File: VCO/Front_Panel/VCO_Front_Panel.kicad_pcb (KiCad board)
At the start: 2 copper layers, 50.3 x 128.5 mm, 5 parts

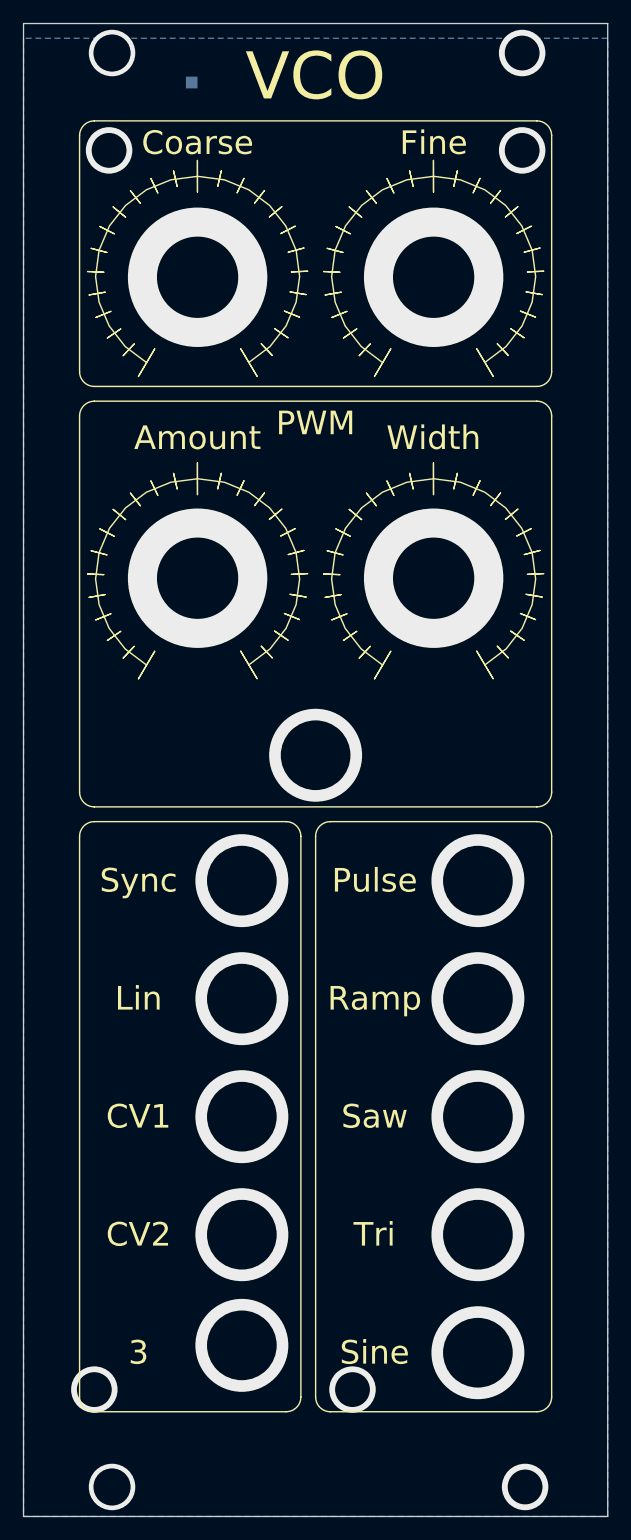
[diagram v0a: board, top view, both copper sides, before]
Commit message: Resolve most of the issues in known_issues.txt
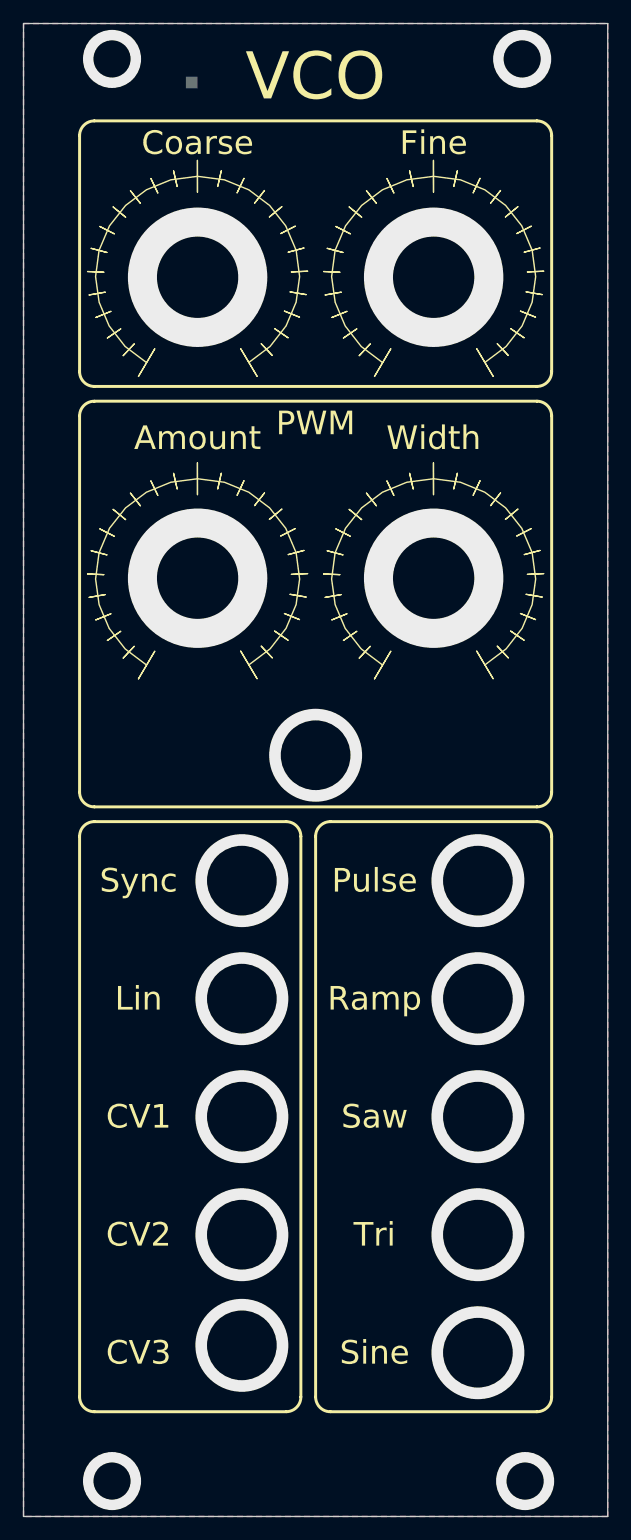
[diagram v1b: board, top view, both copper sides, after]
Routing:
- net GND: vias 23 -> 19
- added copper zone on F.Cu, net GND
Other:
- board text added: "CV3"
- board text removed: "3"

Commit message: Fix minor issues with VCO board
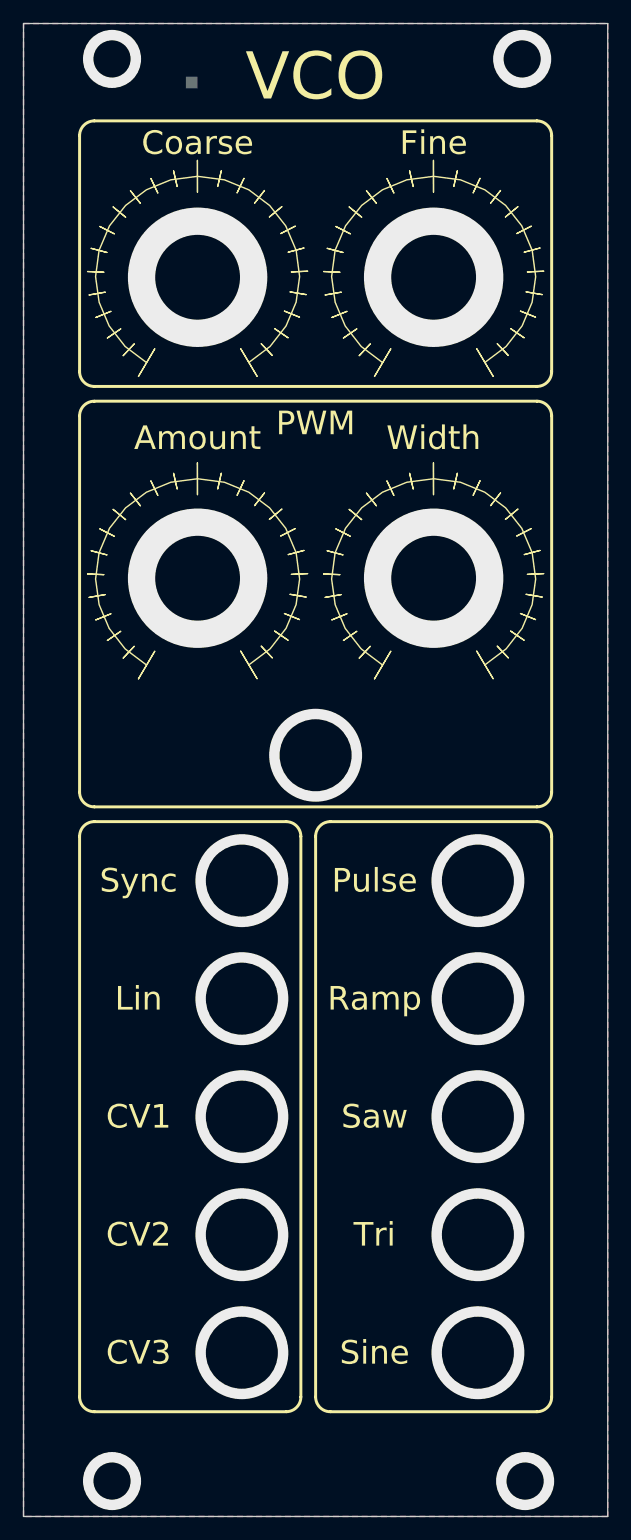
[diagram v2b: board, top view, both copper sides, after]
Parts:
- added REF**: OSHW-Logo2_7.3x6mm_SilkScreen, Symbol:OSHW-Logo2_7.3x6mm_SilkScreen, B.Cu at (97.3, 44.5)
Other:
- board text added: "WH"

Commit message: Bunch of bug fixes and tweaks
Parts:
- removed TP1: TestPoint, TestPoint:TestPoint_Pad_1.0x1.0mm
- added H1: Top_MH1, Eurorack:eurorack_mounting_hole, F.Cu at (71.4, 42.9)
- added H10: Ramp, Eurorack:jack_fp_hole, F.Cu at (102.9, 123.8)
- added H11: Saw, Eurorack:jack_fp_hole, F.Cu at (102.9, 134.0)
- added H12: PWM_Mod, Eurorack:jack_fp_hole, F.Cu at (88.9, 102.9)
- added H13: CV1, Eurorack:jack_fp_hole, F.Cu at (82.5, 134.0)
- added H14: Tri, Eurorack:jack_fp_hole, F.Cu at (102.9, 144.1)
- added H15: CV2, Eurorack:jack_fp_hole, F.Cu at (82.5, 144.1)
- added H16: Sine, Eurorack:jack_fp_hole, F.Cu at (102.9, 154.3)
- added H17: CV3, Eurorack:jack_fp_hole, F.Cu at (82.5, 154.3)
- added H18: Top_MH2, Eurorack:eurorack_mounting_hole, F.Cu at (106.7, 42.9)
- added H19: Bottom_MH2, Eurorack:eurorack_mounting_hole, F.Cu at (106.9, 165.4)
- added H2: Bottom_MH1, Eurorack:eurorack_mounting_hole, F.Cu at (71.4, 165.4)
- added H3: Coarse, Eurorack:pot_fp_hole, F.Cu at (78.7, 61.7)
- added H4: PWM_Amt, Eurorack:pot_fp_hole, F.Cu at (78.7, 87.6)
- added H5: Sync, Eurorack:jack_fp_hole, F.Cu at (82.5, 113.7)
- added H6: Pulse, Eurorack:jack_fp_hole, F.Cu at (102.9, 113.7)
- added H7: Fine, Eurorack:pot_fp_hole, F.Cu at (99.1, 61.7)
- added H8: PWM_Width, Eurorack:pot_fp_hole, F.Cu at (99.1, 87.6)
- added H9: Lin, Eurorack:jack_fp_hole, F.Cu at (82.5, 123.8)
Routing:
- net GND: vias 19 -> 0

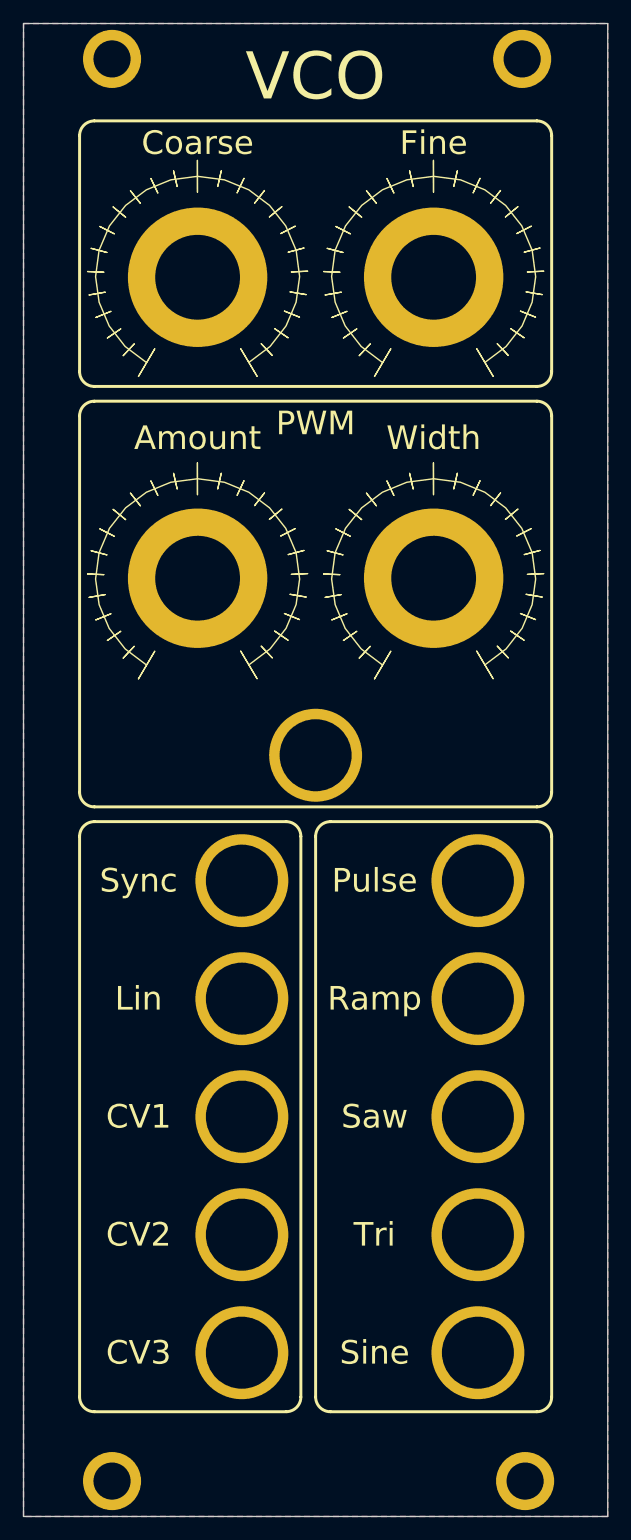
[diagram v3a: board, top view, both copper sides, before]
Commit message: Clean up layout of VCO board
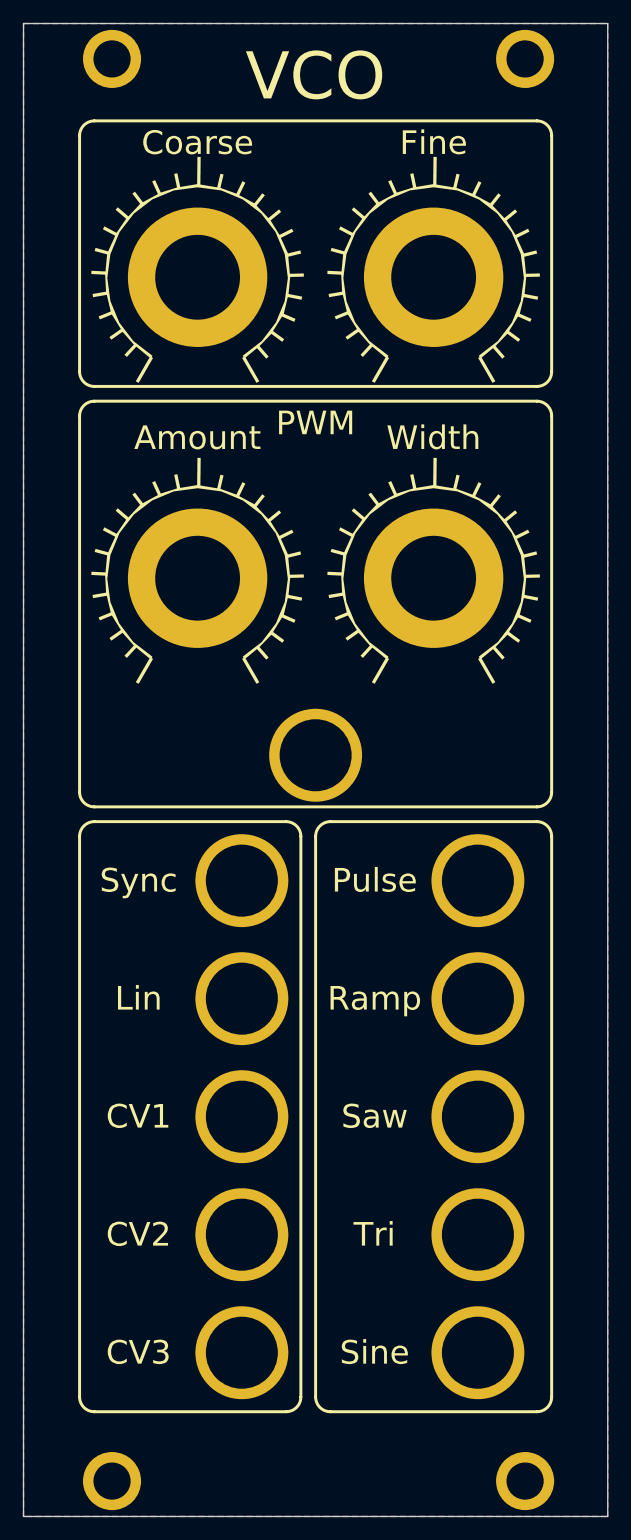
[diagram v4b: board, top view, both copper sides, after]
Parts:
- removed tick_marks (x4): G***, AS3340_VCO_FP:knob_tick_marks
- added svg2mod: G***, Eurorack:knob_tick_marks, F.Cu at (78.7, 87.0)
- added svg2mod: G***, Eurorack:knob_tick_marks, F.Cu at (99.1, 87.0)
- added svg2mod: G***, Eurorack:knob_tick_marks, F.Cu at (78.7, 61.1)
- added svg2mod: G***, Eurorack:knob_tick_marks, F.Cu at (99.1, 61.1)
- moved H18 0.25 mm to (106.9, 42.9)
